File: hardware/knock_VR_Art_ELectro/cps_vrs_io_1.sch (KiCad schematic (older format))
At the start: 38 parts, among them P1 CONN_2, P2 CONN_2, P3 CONN_5X2, P31 CONN_1, P32 CONN_1, P4 CONN_4, U20 MAX9926/9927, U24 MAX9939

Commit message: v 2
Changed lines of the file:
@@
 LIBS:siliconi
 LIBS:contrib
-EELAYER 24 0
+LIBS:cps_vrs_io_1-cache
+EELAYER 27 0
 EELAYER END
 $Descr B 17000 11000
@@
 Sheet 1 1
 Title "cps_vrs_io_1"
-Date "18 nov 2013"
+Date "24 nov 2013"
 Rev ""
 Comp "based on http://code.google.com/p/daecu/"
@@
 	11000 2425 10375 2425
 Wire Wire Line
-	14775 1825 14250 1825
+	14250 1825 14775 1825
 Wire Bus Line
 	1000 1650 1000 3525
@@
 	12250 2925 12250 2825
 Wire Wire Line
-	12750 2525 12750 2925
+	12750 2925 12750 2525
 Connection ~ 12600 1425
 Wire Wire Line
@@
 Connection ~ 12750 2225
 Wire Wire Line
-	12750 2350 12750 2125
+	12750 2125 12750 2350
 Wire Wire Line
 	12100 1925 12750 1925
@@
 Connection ~ 12250 1425
 Wire Wire Line
-	12750 2925 12100 2925
+	12100 2925 12750 2925
 Connection ~ 12600 2925
 Wire Wire Line
@@
 $EndComp
 Wire Bus Line
-	2950 5600 2950 850
+	2950 850  2950 5600
 Wire Wire Line
 	5450 2100 5725 2100
@@
 Wire Wire Line
 	7675 1800 7250 1800
-Connection ~ 8325 1800
+Connection ~ 8300 1800
 Wire Wire Line
 	6925 2300 7000 2300
@@
 	8650 2400 8650 2500
 Wire Wire Line
-	8075 1575 8325 1575
-Wire Wire Line
-	8325 1575 8325 1925
+	8075 1575 8300 1575
+Wire Wire Line
+	8300 1500 8300 1925
 Wire Wire Line
 	7675 1575 7250 1575
@@
 L GND #PWR05
 U 1 1 4E39E4F8
-P 8325 1925
-F 0 "#PWR05" H 8325 1925 30  0001 C CNN
-F 1 "GND" H 8325 1855 30  0001 C CNN
-F 2 "" H 8325 1925 60  0001 C CNN
-F 3 "" H 8325 1925 60  0001 C CNN
-	1    8325 1925
+P 8300 1925
+F 0 "#PWR05" H 8300 1925 30  0001 C CNN
+F 1 "GND" H 8300 1855 30  0001 C CNN
+F 2 "" H 8300 1925 60  0001 C CNN
+F 3 "" H 8300 1925 60  0001 C CNN
+	1    8300 1925
 	1    0    0    -1
 $EndComp
@@
 	0    1    1    0
 $EndComp
+$Comp
+L PWR_FLAG #FLG09
+U 1 1 5291FC2F
+P 8300 1500
+F 0 "#FLG09" H 8300 1595 30  0001 C CNN
+F 1 "PWR_FLAG" H 8300 1680 30  0000 C CNN
+F 2 "" H 8300 1500 60  0000 C CNN
+F 3 "" H 8300 1500 60  0000 C CNN
+	1    8300 1500
+	1    0    0    -1
+$EndComp
+Connection ~ 8300 1575
 $EndSCHEMATC

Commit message: with LED
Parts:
- added D1: LED, SM0805, symbol LED
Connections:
- wire segments 91 -> 94
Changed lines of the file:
@@
 LIBS:contrib
 LIBS:cps_vrs_io_1-cache
-EELAYER 27 0
+EELAYER 24 0
 EELAYER END
 $Descr B 17000 11000
@@
 Sheet 1 1
 Title "cps_vrs_io_1"
-Date "24 nov 2013"
+Date "25 nov 2013"
 Rev ""
 Comp "based on http://code.google.com/p/daecu/"
@@
 $EndComp
 Connection ~ 8300 1575
+$Comp
+L LED D1
+U 1 1 529380F6
+P 11450 3300
+F 0 "D1" H 11450 3400 50  0000 C CNN
+F 1 "LED" H 11450 3200 50  0000 C CNN
+F 2 "SM0805" H 11450 3300 60  0001 C CNN
+F 3 "" H 11450 3300 60  0000 C CNN
+	1    11450 3300
+	0    1    1    0
+$EndComp
+$Comp
+L GND #PWR010
+U 1 1 52938112
+P 11450 3500
+F 0 "#PWR010" H 11450 3500 30  0001 C CNN
+F 1 "GND" H 11450 3430 30  0001 C CNN
+F 2 "" H 11450 3500 60  0001 C CNN
+F 3 "" H 11450 3500 60  0001 C CNN
+	1    11450 3500
+	-1   0    0    -1
+$EndComp
+Wire Wire Line
+	11400 2725 11400 2825
+Wire Wire Line
+	11400 2825 11450 2825
+Wire Wire Line
+	11450 2825 11450 3100
 $EndSCHEMATC

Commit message: 
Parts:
- removed JP1: JUMPER3, SIL-3, symbol JUMPER3
- removed P1, P2: CONN_2, bornier2, symbol CONN_2
- removed P31, P32: CONN_1, SIL-1, symbol CONN_1
- removed R37: 1K, SM0805, symbol R
- removed W1, W2, W3: JMP, SIL-2, symbol TEST
- added D2: LED, SM0805, symbol LED
- added P1, P2: CONN_1, PIN_ARRAY_1, symbol CONN_1
- added R1: 1K, SM0805, symbol R
- P4: footprint bornier4 -> PIN_ARRAY_4x1
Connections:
- net labels added: 5v stab
- net labels removed: CRK1+, FAKE-CAM, RPMGEN_0, RPMGEN_1
- wire segments 94 -> 81
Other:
- note removed: "100pF"
- note removed: "1nF"
- note removed: "20k"
- note removed: "AN00"
- note removed: "AN01"
- note removed: "INSTALL JUMPER TO CONNECT\nCAM GENERATOR TO \nCAM DECODER"
- note removed: "INSTALL JUMPER TO CONNECT\nCRANK GENERATOR TO \nCRANK DECODER"
- note removed: "INSTALL JUMPER TO CONNECT\nFAKE CAM TO\nCAM DECODER\nWASTED SPARK ONLY\nCRANK SENSOR ONLY"
- moved on the sheet: D1, P3, R41

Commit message: now with logo
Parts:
- added G1: LOGO, symbol LOGO
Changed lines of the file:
@@
 LIBS:siliconi
 LIBS:contrib
+LIBS:logo_flipped
 LIBS:cps_vrs_io_1-cache
-EELAYER 24 0
+EELAYER 27 0
 EELAYER END
 $Descr B 17000 11000
@@
 Sheet 1 1
 Title "cps_vrs_io_1"
-Date "02 Dec 2013"
+Date "2 dec 2013"
 Rev ""
 Comp "based on http://code.google.com/p/daecu/"
@@
 Wire Bus Line
 	2600 850  2975 850
+$Comp
+L LOGO G1
+U 1 1 529CF98B
+P 8150 5650
+F 0 "G1" H 8150 5547 60  0001 C CNN
+F 1 "LOGO" H 8150 5753 60  0001 C CNN
+F 2 "" H 8150 5650 60  0000 C CNN
+F 3 "" H 8150 5650 60  0000 C CNN
+	1    8150 5650
+	1    0    0    -1
+$EndComp
 $EndSCHEMATC

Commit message: 
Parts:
- C10: footprint SM1206 -> SM0805
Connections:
- net CRK2+: now reaches P4.4 (P4), R38.1
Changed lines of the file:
@@
 LIBS:contrib
 LIBS:logo_flipped
+LIBS:logo
 LIBS:cps_vrs_io_1-cache
-EELAYER 27 0
+EELAYER 24 0
 EELAYER END
 $Descr B 17000 11000
@@
 Sheet 1 1
 Title "cps_vrs_io_1"
-Date "2 dec 2013"
+Date "3 dec 2013"
 Rev ""
 Comp "based on http://code.google.com/p/daecu/"
@@
 Wire Wire Line
 	14250 1825 14775 1825
-Connection ~ -4675 3450
 Connection ~ 12250 2425
 Wire Wire Line
@@
 F 0 "C10" H 14325 1525 50  0000 L CNN
 F 1 "10uF" H 14025 1725 50  0000 L CNN
-F 2 "SM1206" V 12605 3425 60  0001 C CNN
+F 2 "SM0805" V 12605 3425 60  0001 C CNN
 F 3 "" H 14250 1625 60  0001 C CNN
 F 4 "Taiyo,TMK316BJ106KL-T" V 12605 3425 60  0001 C CNN "mfg,mfg#"
@@
 	1    0    0    -1
 $EndComp
+Text Label 11000 1425 2    60   ~ 0
+CRK2+
 $EndSCHEMATC

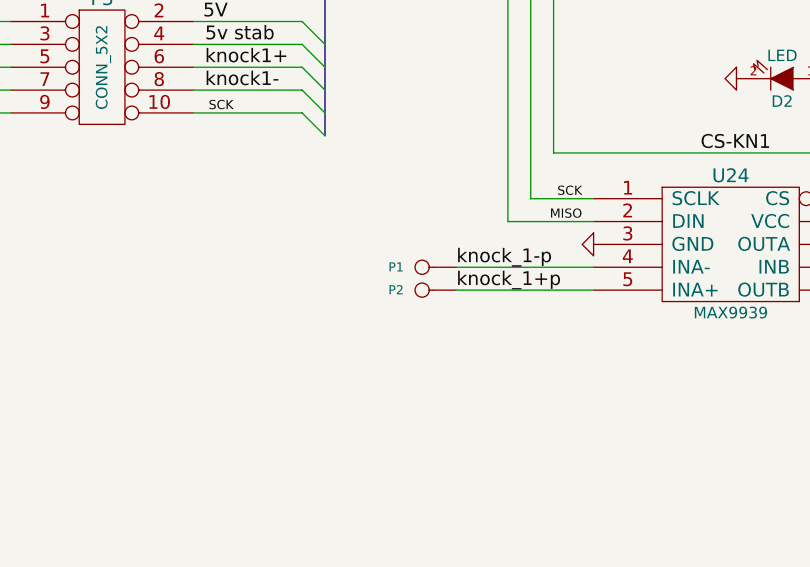
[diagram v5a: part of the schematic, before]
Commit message: 
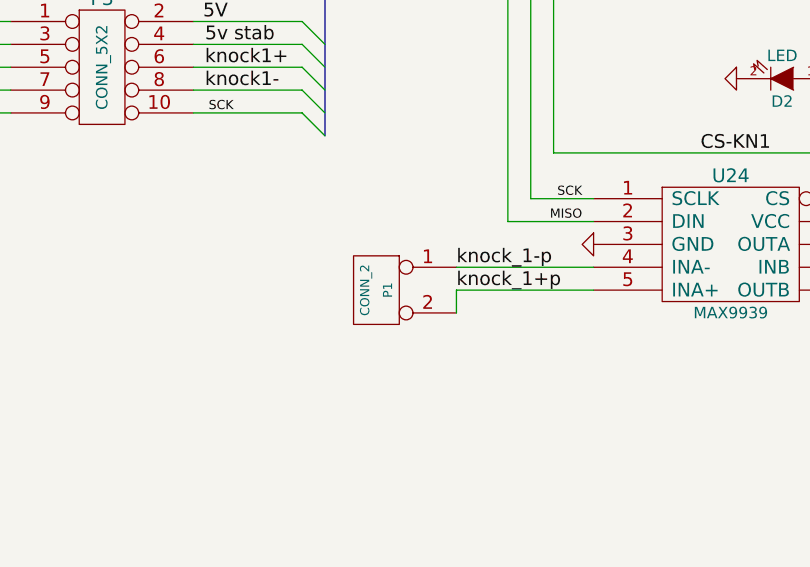
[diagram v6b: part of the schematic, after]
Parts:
- removed P1, P2: CONN_1, PIN_ARRAY_1, symbol CONN_1
- added P1: CONN_2, symbol CONN_2
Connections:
- net knock_1+p: now also P1.2 (PM)
- net knock_1-p: now also P1.1 (P1)
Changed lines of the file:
@@
 LIBS:logo_flipped
 LIBS:logo
+LIBS:art-electro-conn
 LIBS:cps_vrs_io_1-cache
 EELAYER 24 0
@@
 Sheet 1 1
 Title "cps_vrs_io_1"
-Date "3 dec 2013"
+Date "10 Dec 2013"
 Rev ""
 Comp "based on http://code.google.com/p/daecu/"
@@
 $EndComp
 Connection ~ 14250 1150
-$Comp
-L CONN_1 P1
-U 1 1 529C78A8
-P 4975 2400
-F 0 "P1" H 5055 2400 40  0000 L CNN
-F 1 "CONN_1" H 4975 2455 30  0001 C CNN
-F 2 "PIN_ARRAY_1" H 4975 2400 60  0001 C CNN
-F 3 "" H 4975 2400 60  0000 C CNN
-	1    4975 2400
-	-1   0    0    1
-$EndComp
-$Comp
-L CONN_1 P2
-U 1 1 529C79C8
-P 4975 2500
-F 0 "P2" H 5055 2500 40  0000 L CNN
-F 1 "CONN_1" H 4975 2555 30  0001 C CNN
-F 2 "PIN_ARRAY_1" H 4975 2500 60  0001 C CNN
-F 3 "" H 4975 2500 60  0000 C CNN
-	1    4975 2500
-	-1   0    0    1
-$EndComp
 Wire Bus Line
 	4550 850  4550 1825
@@
 Text Label 11000 1425 2    60   ~ 0
 CRK2+
+$Comp
+L CONN_2 P1
+U 1 1 52A72119
+P 4775 2500
+F 0 "P1" V 4725 2500 40  0000 C CNN
+F 1 "CONN_2" V 4825 2500 40  0000 C CNN
+F 2 "" H 4775 2500 60  0000 C CNN
+F 3 "" H 4775 2500 60  0000 C CNN
+	1    4775 2500
+	-1   0    0    -1
+$EndComp
+Wire Wire Line
+	5125 2500 5125 2600
 $EndSCHEMATC

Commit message: remaning components
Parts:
- renumbered C5 to C101, C6 to C102, C10 to C103, C13 to C104, C31 to C105, C32 to C106, C33 to C107, C34 to C108, D1 to D101, D2 to D102, G1 to G101, P1 to P101, P3 to P103, P4 to P104, R1 to R101, R38 to R102, R39 to R103, R40 to R104, R41 to R105, R42 to R106, R43 to R107, R44 to R108, R45 to R109, R46 to R110, R48 to R111, R49 to R112, R52 to R113, R53 to R114, R62 to R115, R64 to R116, R65 to R117, R66 to R118, U20 to U101, U24 to U102
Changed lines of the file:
@@
 	10175 3525 10175 1425
 $Comp
-L C C13
+L C C104
 U 1 1 50D6291F
 P 14775 1625
-F 0 "C13" H 14600 1725 50  0000 L CNN
+F 0 "C104" H 14600 1725 50  0000 L CNN
 F 1 "0.1uF" H 14525 1525 50  0000 L CNN
 F 2 "SM0805" V 880 2900 60  0001 C CNN
@@
 NoConn ~ 14250 1925
 $Comp
-L R R43
+L R R107
 U 1 1 4E39E3AD
 P 11850 1425
-F 0 "R43" V 11930 1425 50  0000 C CNN
+F 0 "R107" V 11930 1425 50  0000 C CNN
 F 1 "5k" V 11850 1425 50  0000 C CNN
 F 2 "SM0805" V 880 2900 60  0001 C CNN
@@
 $EndComp
 $Comp
-L R R38
+L R R102
 U 1 1 4E39E3A9
 P 11250 1425
-F 0 "R38" V 11330 1425 50  0000 C CNN
+F 0 "R102" V 11330 1425 50  0000 C CNN
 F 1 "5k" V 11250 1425 50  0000 C CNN
 F 2 "SM0805" V 880 2900 60  0001 C CNN
@@
 $EndComp
 $Comp
-L R R39
+L R R103
 U 1 1 4E39E3A5
 P 11250 1925
-F 0 "R39" V 11150 1925 50  0000 C CNN
+F 0 "R103" V 11150 1925 50  0000 C CNN
 F 1 "5k" V 11250 1925 50  0000 C CNN
 F 2 "SM0805" V 880 2900 60  0001 C CNN
@@
 $EndComp
 $Comp
-L R R44
+L R R108
 U 1 1 4E39E3A0
 P 11850 1925
-F 0 "R44" V 11750 1925 50  0000 C CNN
+F 0 "R108" V 11750 1925 50  0000 C CNN
 F 1 "5k" V 11850 1925 50  0000 C CNN
 F 2 "SM0805" V 880 2900 60  0001 C CNN
@@
 $EndComp
 $Comp
-L R R42
+L R R106
 U 1 1 4E39E39D
 P 11250 2925
-F 0 "R42" V 11330 2925 50  0000 C CNN
+F 0 "R106" V 11330 2925 50  0000 C CNN
 F 1 "5k" V 11250 2925 50  0000 C CNN
 F 2 "SM0805" V 880 2900 60  0001 C CNN
@@
 $EndComp
 $Comp
-L R R40
+L R R104
 U 1 1 4E39E39B
 P 11250 2425
-F 0 "R40" V 11330 2425 50  0000 C CNN
+F 0 "R104" V 11330 2425 50  0000 C CNN
 F 1 "5k" V 11250 2425 50  0000 C CNN
 F 2 "SM0805" V 880 2900 60  0001 C CNN
@@
 $EndComp
 $Comp
-L R R41
+L R R105
 U 1 1 4E39E399
 P 14000 1150
-F 0 "R41" V 14080 1150 50  0000 C CNN
+F 0 "R105" V 14080 1150 50  0000 C CNN
 F 1 "1K" V 14000 1150 50  0000 C CNN
 F 2 "SM0805" V 3630 1325 60  0001 C CNN
@@
 $EndComp
 $Comp
-L R R45
+L R R109
 U 1 1 4E39E396
 P 11850 2425
-F 0 "R45" V 11930 2425 50  0000 C CNN
+F 0 "R109" V 11930 2425 50  0000 C CNN
 F 1 "5k" V 11850 2425 50  0000 C CNN
 F 2 "SM0805" V 880 2900 60  0001 C CNN
@@
 $EndComp
 $Comp
-L R R46
+L R R110
 U 1 1 4E39E393
 P 11850 2925
-F 0 "R46" V 11930 2925 50  0000 C CNN
+F 0 "R110" V 11930 2925 50  0000 C CNN
 F 1 "5k" V 11850 2925 50  0000 C CNN
 F 2 "SM0805" V 880 2900 60  0001 C CNN
@@
 $EndComp
 $Comp
-L R R48
+L R R111
 U 1 1 4E39E390
 P 12600 1675
-F 0 "R48" V 12680 1675 50  0000 C CNN
+F 0 "R111" V 12680 1675 50  0000 C CNN
 F 1 "5k" V 12600 1675 50  0000 C CNN
 F 2 "SM0805" V 880 2900 60  0001 C CNN
@@
 $EndComp
 $Comp
-L R R49
+L R R112
 U 1 1 4E39E38D
 P 12600 2675
-F 0 "R49" V 12680 2675 50  0000 C CNN
+F 0 "R112" V 12680 2675 50  0000 C CNN
 F 1 "5k" V 12600 2675 50  0000 C CNN
 F 2 "SM0805" V 880 2900 60  0001 C CNN
@@
 $EndComp
 $Comp
-L MAX9926/9927 U20
+L MAX9926/9927 U101
 U 1 1 4BF90B79
 P 13500 2175
-F 0 "U20" H 13500 2625 60  0000 C CNN
+F 0 "U101" H 13500 2625 60  0000 C CNN
 F 1 "MAX9926/9927" V 13400 2175 50  0000 C CNN
 F 2 "maxim-10-QSOP16" H 13500 2175 60  0001 C CNN
@@
 $EndComp
 $Comp
-L R R53
+L R R114
 U 1 1 5101D08D
 P 15050 2225
-F 0 "R53" V 15130 2225 50  0000 C CNN
+F 0 "R114" V 15130 2225 50  0000 C CNN
 F 1 "10k" V 15050 2225 50  0000 C CNN
 F 2 "SM0805" V 880 2900 60  0001 C CNN
@@
 $EndComp
 $Comp
-L C C6
+L C C102
 U 1 1 4AD9CD25
 P 12250 2625
-F 0 "C6" H 12350 2725 50  0000 L CNN
+F 0 "C102" H 12350 2725 50  0000 L CNN
 F 1 "1000pF" H 12250 2525 50  0000 L CNN
 F 2 "SM0805" V 880 2900 60  0001 C CNN
@@
 $EndComp
 $Comp
-L C C10
+L C C103
 U 1 1 4AD9CB8E
 P 14250 1625
-F 0 "C10" H 14325 1525 50  0000 L CNN
+F 0 "C103" H 14325 1525 50  0000 L CNN
 F 1 "10uF" H 14025 1725 50  0000 L CNN
 F 2 "SM0805" V 12605 3425 60  0001 C CNN
@@
 $EndComp
 $Comp
-L C C5
+L C C101
 U 1 1 4AD9C851
 P 12250 1725
-F 0 "C5" H 12300 1825 50  0000 L CNN
+F 0 "C101" H 12300 1825 50  0000 L CNN
 F 1 "1000pF" H 12250 1625 50  0000 L CNN
 F 2 "SM0805" V 880 2900 60  0001 C CNN
@@
 $EndComp
 $Comp
-L R R52
+L R R113
 U 1 1 4AD9C75B
 P 15050 2125
-F 0 "R52" V 15130 2125 50  0000 C CNN
+F 0 "R113" V 15130 2125 50  0000 C CNN
 F 1 "10k" V 15050 2125 50  0000 C CNN
 F 2 "SM0805" V 880 2900 60  0001 C CNN
@@
 SCK
 $Comp
-L R R64
+L R R116
 U 1 1 4E39E500
 P 7750 2400
-F 0 "R64" V 7650 2400 50  0000 C CNN
+F 0 "R116" V 7650 2400 50  0000 C CNN
 F 1 "10K" V 7750 2400 50  0000 C CNN
 F 2 "SM0805" V -195 400 60  0001 C CNN
@@
 $EndComp
 $Comp
-L R R66
+L R R118
 U 1 1 4E39E4FF
 P 8400 2400
-F 0 "R66" V 8500 2400 50  0000 C CNN
+F 0 "R118" V 8500 2400 50  0000 C CNN
 F 1 "20K" V 8400 2400 50  0000 C CNN
 F 2 "SM0805" H 8400 2400 60  0001 C CNN
@@
 $EndComp
 $Comp
-L C C34
+L C C108
 U 1 1 4E39E4FC
 P 8650 2700
-F 0 "C34" H 8375 2800 50  0000 L CNN
+F 0 "C108" H 8375 2800 50  0000 L CNN
 F 1 "1000pF" H 8675 2800 50  0000 L CNN
 F 2 "SM0805" V -195 400 60  0001 C CNN
@@
 $EndComp
 $Comp
-L R R62
+L R R115
 U 1 1 4E39E4F7
 P 7250 2300
-F 0 "R62" V 7400 2275 50  0000 C CNN
+F 0 "R115" V 7400 2275 50  0000 C CNN
 F 1 "10K" V 7250 2300 50  0000 C CNN
 F 2 "SM0805" V -195 400 60  0001 C CNN
@@
 $EndComp
 $Comp
-L R R65
+L R R117
 U 1 1 4E39E4F6
 P 8400 2225
-F 0 "R65" V 8300 2225 50  0000 C CNN
+F 0 "R117" V 8300 2225 50  0000 C CNN
 F 1 "20K" V 8400 2225 50  0000 C CNN
 F 2 "SM0805" H 8400 2225 60  0001 C CNN
@@
 $EndComp
 $Comp
-L C C32
+L C C106
 U 1 1 4E39E4EE
 P 7875 1800
-F 0 "C32" V 7925 2000 50  0000 L CNN
+F 0 "C106" V 7925 2000 50  0000 L CNN
 F 1 "0.1uF" V 7925 1525 50  0000 L CNN
 F 2 "SM0805" V 4480 -1000 60  0001 C CNN
@@
 $EndComp
 $Comp
-L C C31
+L C C105
 U 1 1 4E39E4ED
 P 7875 1575
-F 0 "C31" V 7925 1775 50  0000 L CNN
+F 0 "C105" V 7925 1775 50  0000 L CNN
 F 1 "1uF" V 7925 1375 50  0000 L CNN
 F 2 "SM0805" V 4480 -1000 60  0001 C CNN
@@
 $EndComp
 $Comp
-L C C33
+L C C107
 U 1 1 4E39E4EC
 P 8650 2000
-F 0 "C33" H 8375 2100 50  0000 L CNN
+F 0 "C107" H 8375 2100 50  0000 L CNN
 F 1 "0.1uF" H 8375 1900 50  0000 L CNN
 F 2 "SM0805" V 4480 -1000 60  0001 C CNN
@@
 	5350 2200 5350 950
 $Comp
-L CONN_5X2 P3
+L CONN_5X2 P103
 U 1 1 5288F8BF
 P 3575 1525
-F 0 "P3" H 3575 1825 60  0000 C CNN
+F 0 "P103" H 3575 1825 60  0000 C CNN
 F 1 "CONN_5X2" V 3575 1525 50  0000 C CNN
 F 2 "PIN_ARRAY_5x2" H 3575 1525 60  0001 C CNN
@@
 MISO
 $Comp
-L CONN_4 P4
+L CONN_4 P104
 U 1 1 5288FF50
 P 9400 3375
-F 0 "P4" V 9350 3375 50  0000 C CNN
+F 0 "P104" V 9350 3375 50  0000 C CNN
 F 1 "CONN_4" V 9450 3375 50  0000 C CNN
 F 2 "PIN_ARRAY_4x1" H 9400 3375 60  0001 C CNN
@@
 $EndComp
 $Comp
-L MAX9939 U24
+L MAX9939 U102
 U 1 1 4E39E4FD
 P 6325 2300
-F 0 "U24" H 6325 2600 60  0000 C CNN
+F 0 "U102" H 6325 2600 60  0000 C CNN
 F 1 "MAX9939" H 6325 2000 50  0000 C CNN
 F 2 "uMAX-uSOP_10" H 6325 2300 60  0001 C CNN
@@
 Connection ~ 8300 1575
 $Comp
-L LED D1
+L LED D101
 U 1 1 529380F6
 P 13550 1150
-F 0 "D1" H 13550 1250 50  0000 C CNN
+F 0 "D101" H 13550 1250 50  0000 C CNN
 F 1 "LED" H 13550 1050 50  0000 C CNN
 F 2 "SM0805" H 13550 1150 60  0001 C CNN
@@
 	3175 1625 3125 1625
 $Comp
-L R R1
+L R R101
 U 1 1 529C6F52
 P 7000 1575
-F 0 "R1" V 7080 1575 50  0000 C CNN
+F 0 "R101" V 7080 1575 50  0000 C CNN
 F 1 "1K" V 7000 1575 50  0000 C CNN
 F 2 "SM0805" V -3370 1750 60  0001 C CNN
@@
 $EndComp
 $Comp
-L LED D2
+L LED D102
 U 1 1 529C6F58
 P 6550 1575
-F 0 "D2" H 6550 1675 50  0000 C CNN
+F 0 "D102" H 6550 1675 50  0000 C CNN
 F 1 "LED" H 6550 1475 50  0000 C CNN
 F 2 "SM0805" H 6550 1575 60  0001 C CNN
@@
 	2600 850  2975 850
 $Comp
-L LOGO G1
+L LOGO G101
 U 1 1 529CF98B
 P 8150 5650
-F 0 "G1" H 8150 5547 60  0001 C CNN
+F 0 "G101" H 8150 5547 60  0001 C CNN
 F 1 "LOGO" H 8150 5753 60  0001 C CNN
 F 2 "" H 8150 5650 60  0000 C CNN
@@
 CRK2+
 $Comp
-L CONN_2 P1
+L CONN_2 P101
 U 1 1 52A72119
 P 4775 2500
-F 0 "P1" V 4725 2500 40  0000 C CNN
+F 0 "P101" V 4725 2500 40  0000 C CNN
 F 1 "CONN_2" V 4825 2500 40  0000 C CNN
 F 2 "" H 4775 2500 60  0000 C CNN

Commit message: migrating to external libs
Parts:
- removed D101, D102: LED, SM0805, symbol LED
- added D101, D102: LED, symbol LED_0805
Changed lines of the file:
@@
 EESchema Schematic File Version 2
-LIBS:project_specific_libs
 LIBS:power
 LIBS:device
 LIBS:conn
 LIBS:linear
-LIBS:regul
-LIBS:74xx
-LIBS:cmos4000
-LIBS:adc-dac
-LIBS:memory
-LIBS:xilinx
-LIBS:special
-LIBS:microcontrollers
-LIBS:microchip
-LIBS:analog_switches
-LIBS:motorola
-LIBS:intel
-LIBS:audio
 LIBS:interface
-LIBS:digital-audio
-LIBS:philips
-LIBS:display
-LIBS:cypress
-LIBS:siliconi
-LIBS:contrib
+LIBS:project_specific_libs
 LIBS:logo_flipped
-LIBS:logo
 LIBS:art-electro-conn
 LIBS:cps_vrs_io_1-cache
-EELAYER 24 0
+EELAYER 27 0
 EELAYER END
 $Descr B 17000 11000
@@
 Sheet 1 1
 Title "cps_vrs_io_1"
-Date "10 Dec 2013"
+Date "28 feb 2014"
 Rev ""
 Comp "based on http://code.google.com/p/daecu/"
@@
 Connection ~ 8300 1575
 $Comp
-L LED D101
-U 1 1 529380F6
-P 13550 1150
-F 0 "D101" H 13550 1250 50  0000 C CNN
-F 1 "LED" H 13550 1050 50  0000 C CNN
-F 2 "SM0805" H 13550 1150 60  0001 C CNN
-F 3 "" H 13550 1150 60  0000 C CNN
-	1    13550 1150
-	-1   0    0    1
-$EndComp
-$Comp
 L GND #PWR010
 U 1 1 52938112
@@
 $EndComp
 $Comp
-L LED D102
-U 1 1 529C6F58
-P 6550 1575
-F 0 "D102" H 6550 1675 50  0000 C CNN
-F 1 "LED" H 6550 1475 50  0000 C CNN
-F 2 "SM0805" H 6550 1575 60  0001 C CNN
-F 3 "" H 6550 1575 60  0000 C CNN
-	1    6550 1575
-	-1   0    0    1
-$EndComp
-$Comp
 L GND #PWR011
 U 1 1 529C6F72
@@
 Wire Wire Line
 	5125 2500 5125 2600
+$Comp
+L LED_0805 D102
+U 1 1 53102B67
+P 6550 1575
+F 0 "D102" H 6550 1675 50  0000 C CNN
+F 1 "LED" H 6550 1475 50  0000 C CNN
+F 2 "" H 6550 1575 60  0000 C CNN
+F 3 "" H 6550 1575 60  0000 C CNN
+	1    6550 1575
+	-1   0    0    1
+$EndComp
+$Comp
+L LED_0805 D101
+U 1 1 53102B7E
+P 13550 1150
+F 0 "D101" H 13550 1250 50  0000 C CNN
+F 1 "LED" H 13550 1050 50  0000 C CNN
+F 2 "" H 13550 1150 60  0000 C CNN
+F 3 "" H 13550 1150 60  0000 C CNN
+	1    13550 1150
+	-1   0    0    1
+$EndComp
 $EndSCHEMATC
